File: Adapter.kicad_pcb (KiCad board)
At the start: 6 copper layers, 164.7 x 117 mm, 236 parts, among them J1 GD820HTX75P6HB, J2 2-338069-0, U1 K7805-1000R3, U11 LMV7239M5/NOPB, U2 LM1117GS-5.0, U3 LM1117GS-5.0, U4 LMV7239M5/NOPB, U5 ADuM1200AR, U6 ADuM1200AR, U7 LM1117GS-5.0, U8 LMV7239M5/NOPB, U9 ADuM1200AR

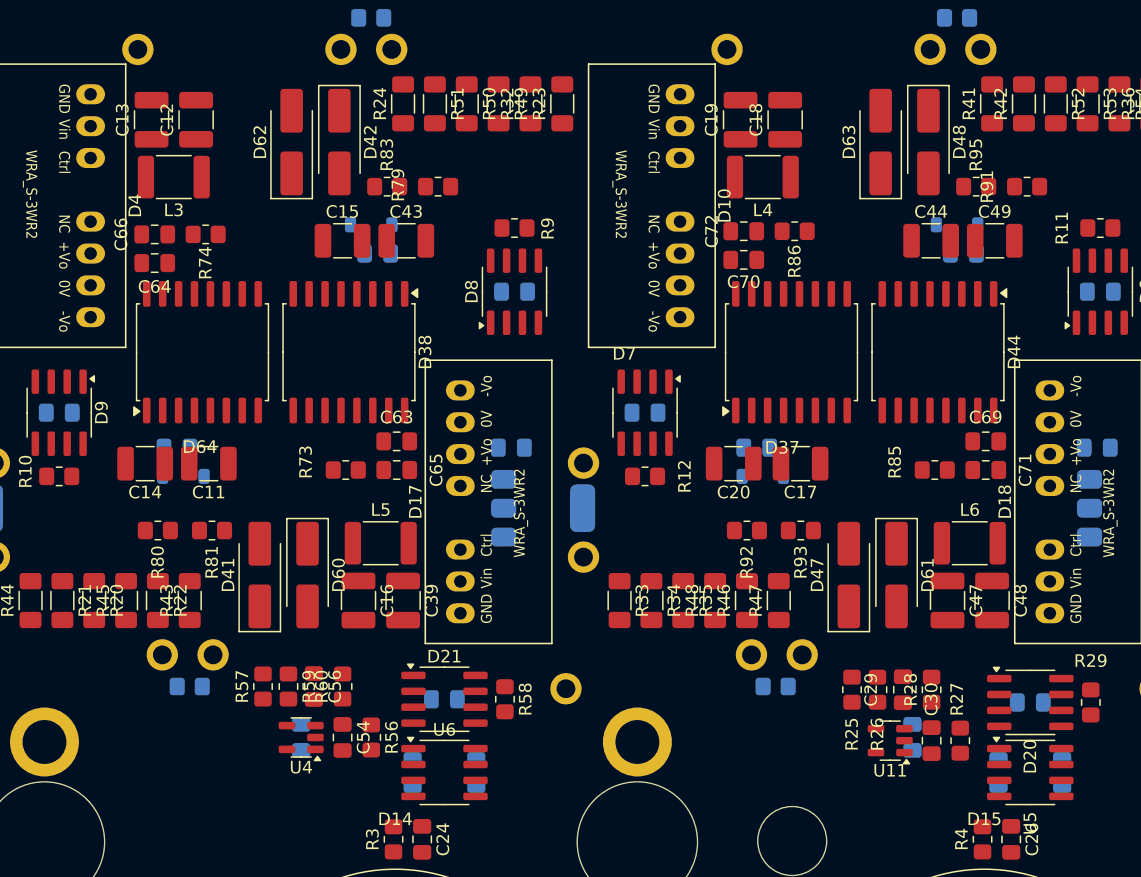
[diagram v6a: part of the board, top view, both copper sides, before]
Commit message: Начал разводить вторую стойку
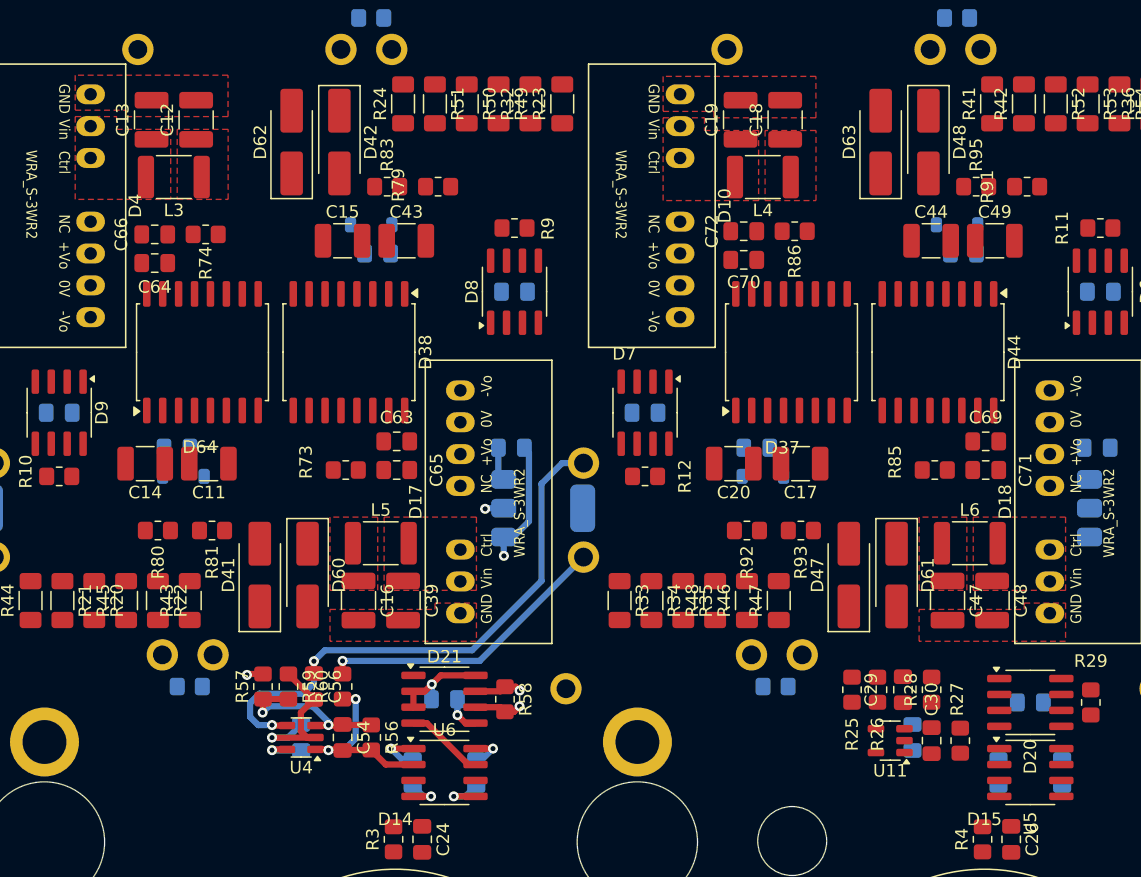
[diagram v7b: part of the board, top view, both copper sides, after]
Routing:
- net T3: track 0.00 -> 45.4 mm, vias 0 -> 2
- net -15V_L1: track 9.19 -> 35.9 mm, vias 2 -> 5
- net T4: track 0.00 -> 23.7 mm, vias 0 -> 1
- net Net-(U6-VIA): track 0.00 -> 15.2 mm, vias 0 -> 2
- net Net-(U4-+): track 0.00 -> 13.9 mm, vias 0 -> 2
- net +5V: track 14.5 -> 25.5 mm, vias 4 -> 6
- net +5V_B: track 0.00 -> 10.2 mm, vias 0 -> 4
- net GND: track 31.4 -> 38.3 mm, vias 8 -> 10
- net Net-(D21-DI): track 0.00 -> 6.32 mm
- net Temp_P: track 0.00 -> 3.85 mm, vias 0 -> 1
- net Temp_N: track 0.00 -> 3.80 mm, vias 0 -> 1
- net E4: track 0.00 -> 2.70 mm
- added copper zone on In1.Cu, net +15V_H2
- added copper zone on In1.Cu, net +15V_H3
- added copper zone on In1.Cu, net +15V_L2
- added copper zone on In1.Cu, net +15V_L3
- added copper zone on In2.Cu, net +5V_B
- added copper zone on In1.Cu, net -15V_H2
- added copper zone on In1.Cu, net -15V_H3
- added copper zone on In2.Cu, net E3
- added copper zone on In2.Cu, net E4
- added copper zone on In2.Cu, net E5
- added copper zone on In2.Cu, net E6
- added copper zone on F.Cu, net Net-(D10-Vin)
- added copper zone on F.Cu, net Net-(D17-Vin)
- added copper zone on F.Cu, net Net-(D18-Vin)
- added copper zone on F.Cu, net Net-(D4-Vin)
